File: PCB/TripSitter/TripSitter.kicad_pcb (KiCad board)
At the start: 6 copper layers, 177 parts, among them IC1 MT25QL256ABA1EW9-0SIT, IC2 MT41J128M16JT-125_K, IC4 IP4220CZ6, J1 Conn_ARM_JTAG_SWD_20, J2 DE15_Plug_HighDensity_Mountin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, J3 Conn_ARM_JTAG_SWD_20, J4 USB_B_Micro, J5 Jack-DC, J6 EFM32_PinHeader_PortE, J7 HDMI_A_1.4, J8 USB3_B_Micro, SW1 SW_Push_Open, SW2 SW_DPDT_x2, SW3 SW_DIP_x05, U1 XC7A100T-FGG484, U2 TPS54325_PWP_14, U3 IS62WVS2568FBLL-20NLI, U4 EFM32GG11B420F2048GQ100, U5 TPS54294PWP, U6 IS62WVS2568FBLL-20NLI, U7 TPD12S520DBT, X1 XO53 100Mhz, Y1 48MHz

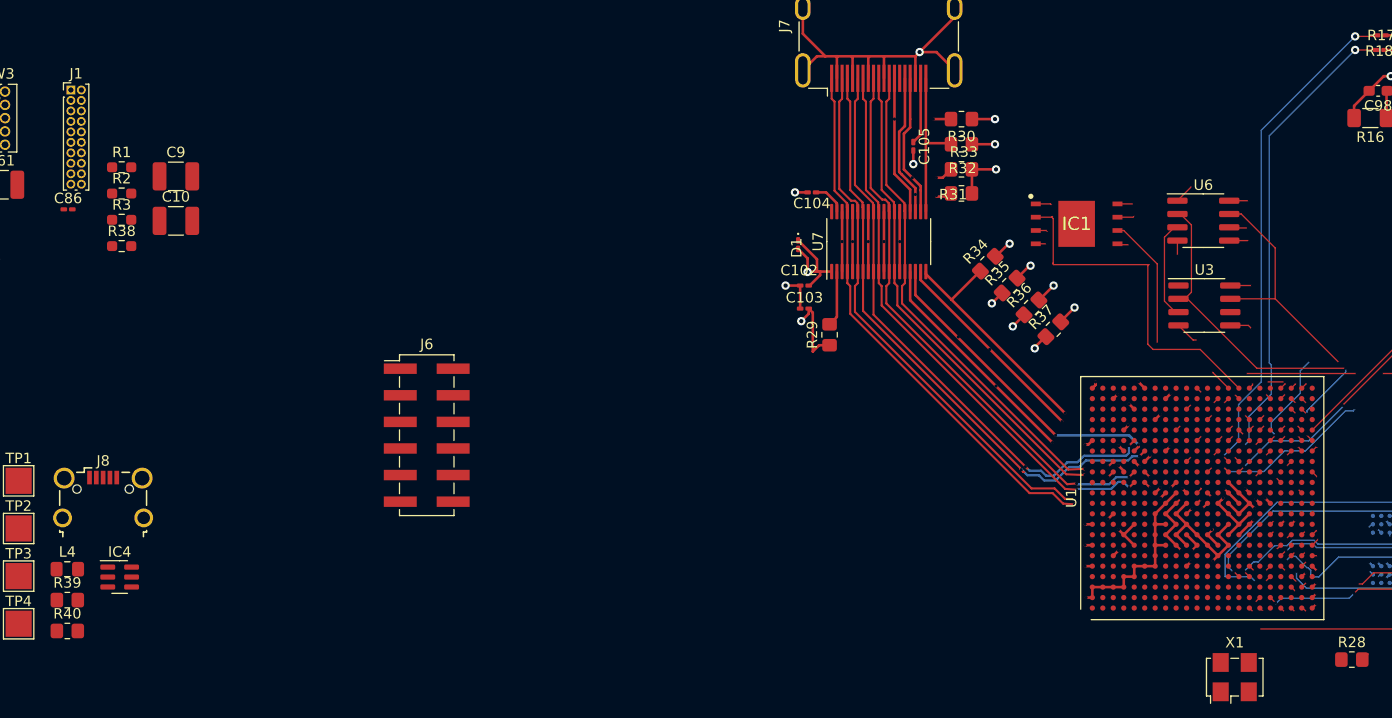
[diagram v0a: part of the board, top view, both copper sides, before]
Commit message: add missing tracks on hdmi
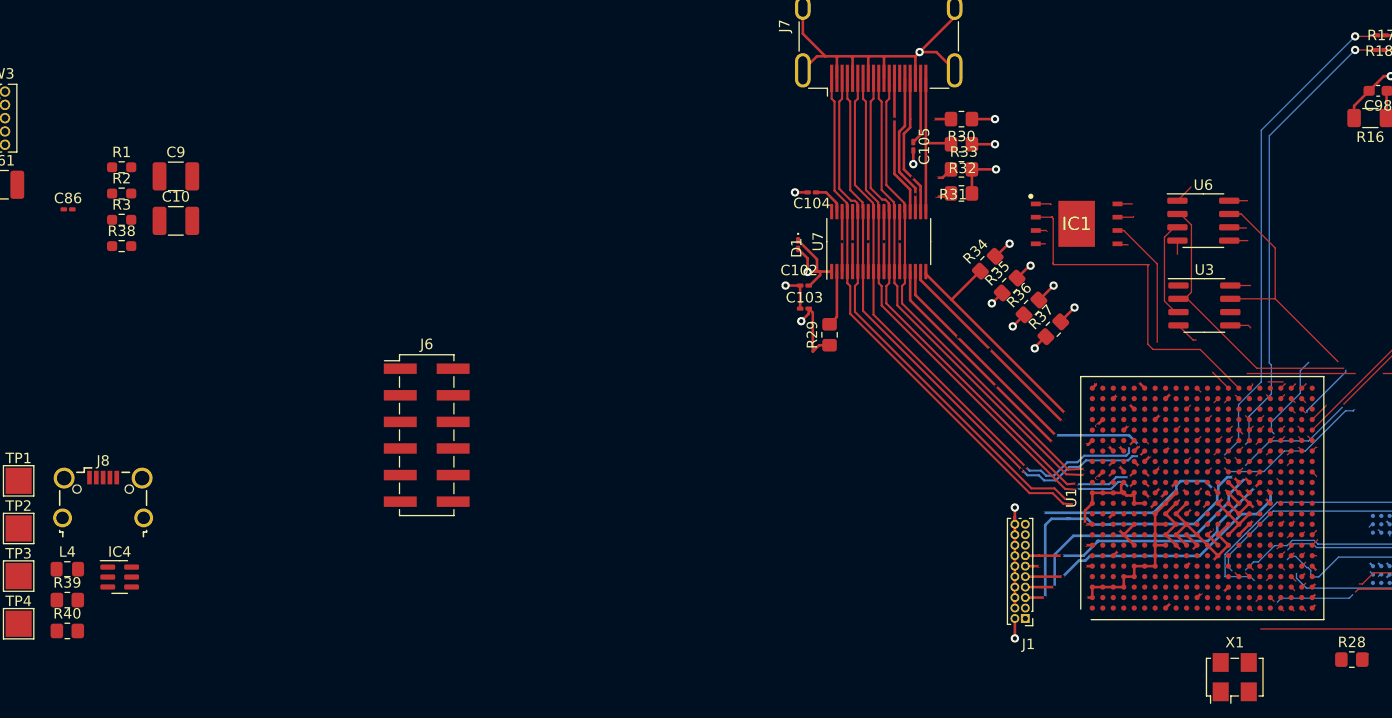
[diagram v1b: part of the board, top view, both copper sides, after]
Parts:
- moved J1 104.2 mm to (213.9, 75.4), turned to 180 degrees
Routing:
- net GND: track 161.7 -> 193.1 mm, vias 44 -> 54
- net Net-(J1-TDI): track 0.00 -> 31.1 mm, vias 0 -> 2
- net Net-(J1-TCK/SWDCLK): track 0.00 -> 28.6 mm, vias 0 -> 2
- net Net-(J1-TMS/SWDIO): track 0.00 -> 28.2 mm, vias 0 -> 2
- net Net-(J1-TDO/SWO): track 0.00 -> 25.8 mm, vias 0 -> 2
- net FPGA_PROGRAM_B: track 0.00 -> 18.7 mm, vias 0 -> 2
- net FPGA_DONE: track 0.00 -> 12.6 mm, vias 0 -> 2
- net +3V3: track 33.9 -> 36.8 mm, vias 28 -> 30
- net +3.3V: track 6.22 -> 7.07 mm, vias 4 -> 5
- net /FPGA Artix-7 100T 1FGG484C/VGA connector/VGA_VSync: track 44.4 -> 45.1 mm

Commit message: Copy/Add power layout
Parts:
- added SW2: SW_DPDT_x2, Button_Switch_SMD:SW_DPDT_CK_JS202011JCQN, F.Cu at (33.9, 48.3)
- moved C101 188.7 mm to (246.1, 145.6)
- moved C28 188.7 mm to (240.5, 138.6)
- moved C30 188.7 mm to (240.5, 140.3)
- moved C31 188.7 mm to (240.5, 142.1)
- moved C32 188.7 mm to (240.5, 143.8)
- moved C42 188.7 mm to (240.5, 145.6)
- moved C43 188.7 mm to (240.5, 147.3)
- moved C44 188.7 mm to (243.3, 138.6)
- moved C45 188.7 mm to (243.3, 140.3)
- moved C80 188.7 mm to (243.3, 142.1)
- moved C81 188.7 mm to (243.3, 143.8)
- moved C82 188.7 mm to (243.3, 145.6)
- moved C83 188.7 mm to (243.3, 147.3)
- moved C90 188.7 mm to (246.1, 138.6)
- moved C91 188.7 mm to (246.1, 140.3)
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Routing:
- net /PCB Power System/5V0: track 0.00 -> 123.7 mm, vias 0 -> 2
- net GND: track 193.1 -> 286.3 mm, vias 54 -> 85
- net /PCB Power System/1V8: track 0.00 -> 75.8 mm, vias 0 -> 1
- net /PCB Power System/1V0: track 0.00 -> 50.8 mm, vias 0 -> 1
- net Net-(U2-PG): track 0.00 -> 31.2 mm
- net /PCB Power System/1V5: track 0.00 -> 26.1 mm, vias 0 -> 1
- net /PCB Power System/3V3: track 0.00 -> 24.8 mm, vias 0 -> 1
- net Net-(U5-VFB2): track 0.00 -> 17.3 mm
- net Net-(U5-EN2): track 0.00 -> 15.5 mm
- net Net-(J4-VBUS): track 0.00 -> 10.7 mm
- net Net-(U2-VREG5): track 0.00 -> 10.3 mm
- net Net-(U2-VFB): track 0.00 -> 8.60 mm
- net Net-(SW2A-C): track 0.00 -> 8.24 mm
- net Net-(U5-VREG5): track 0.00 -> 5.45 mm
- net Net-(U5-SW2): track 0.00 -> 4.12 mm
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
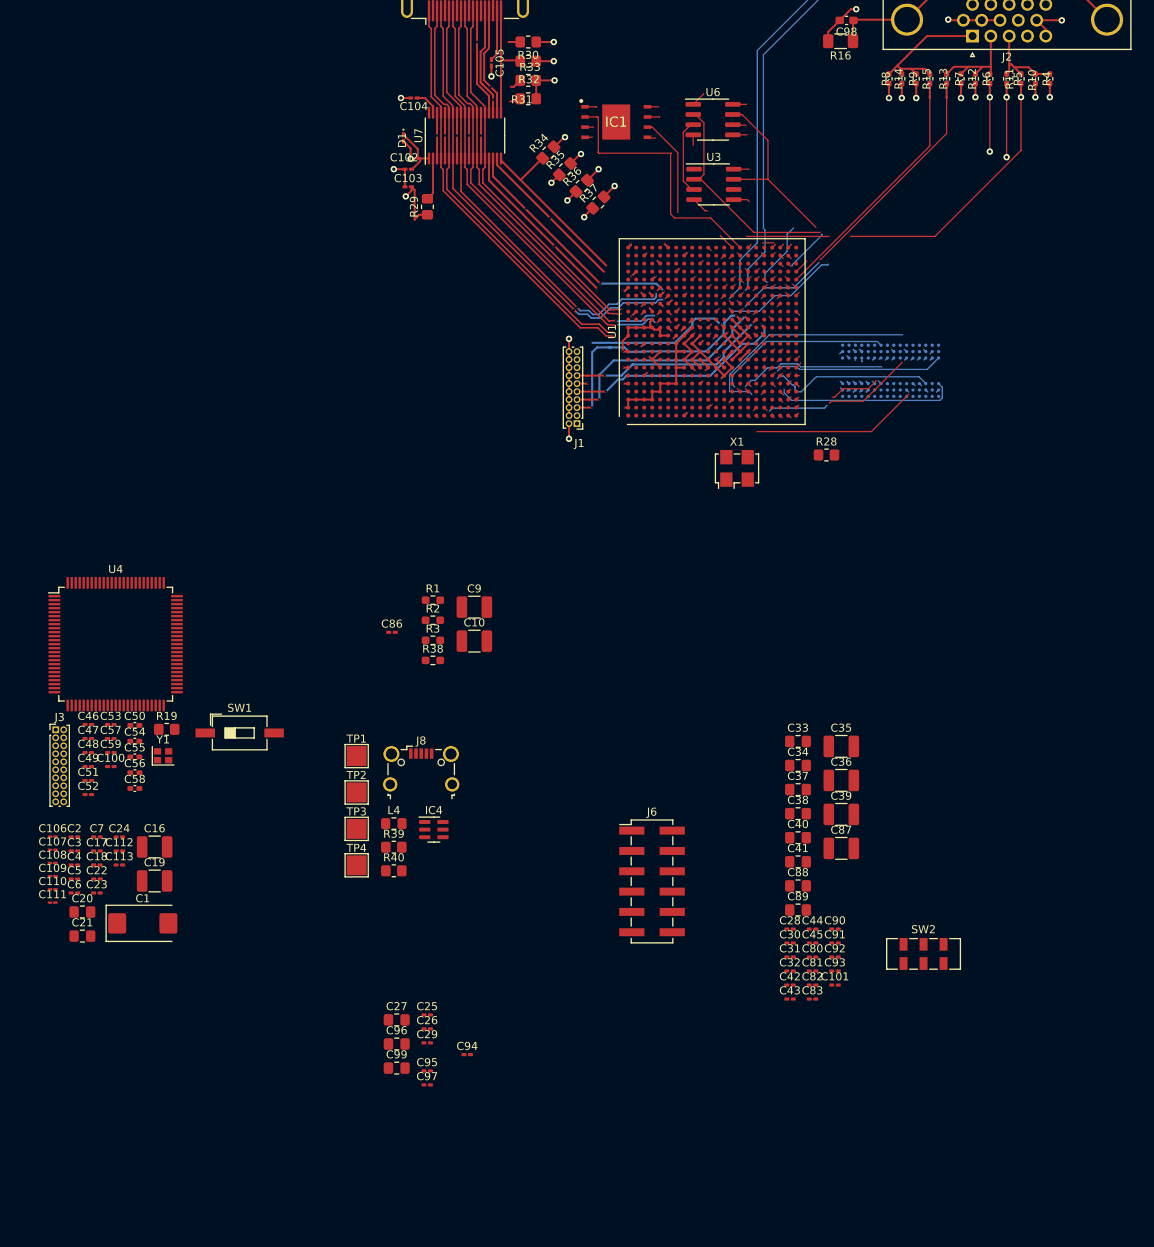
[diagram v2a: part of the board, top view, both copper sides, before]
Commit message: Add USB and JTAG debug for EFM
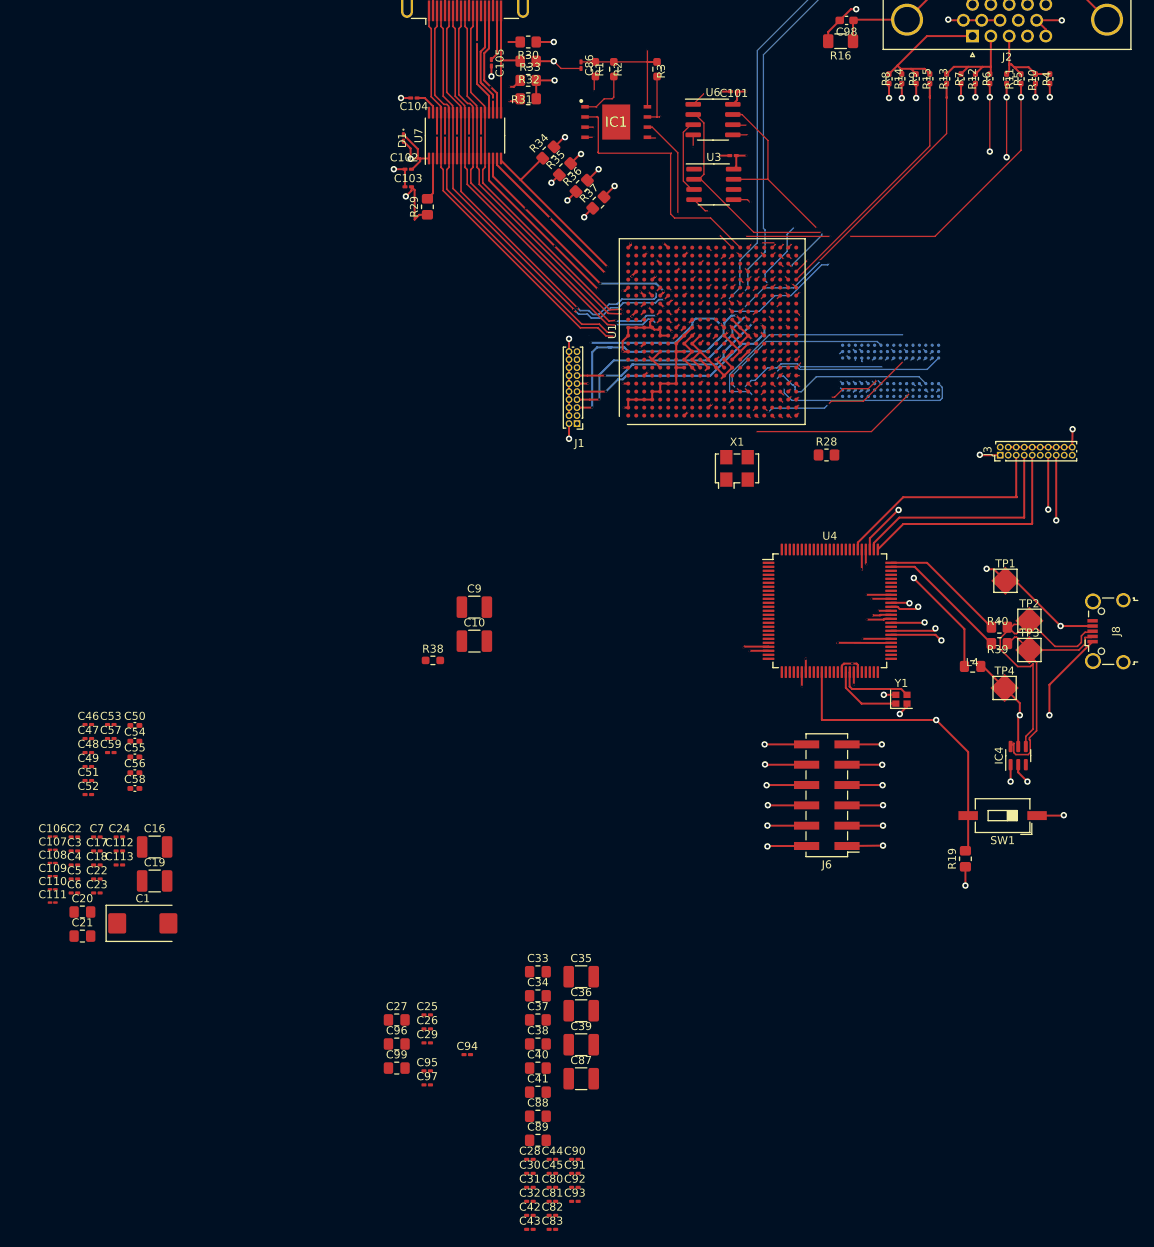
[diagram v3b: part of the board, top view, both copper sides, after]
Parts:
- removed the SW2 at (257.2, 141.7)
- moved J3 123.0 mm to (266.8, 79.3), turned to 90 degrees
- moved C101 112.4 mm to (233.5, 33.9), turned to 180 degrees
- moved C100 109.0 mm to (233.4, 41.9), turned to 180 degrees
- moved R19 101.1 mm to (262.4, 129.8), turned to 90 degrees
- moved SW1 95.9 mm to (267.1, 124.4), turned to 180 degrees
- moved Y1 92.6 mm to (254.4, 109.8)
- moved U4 89.4 mm to (245.5, 98.8)
- moved J8 87.5 mm to (280.2, 101.4), turned to 90 degrees
- moved TP3 87.0 mm to (270.4, 103.7)
- moved TP2 86.8 mm to (270.4, 100.0)
- moved TP1 84.0 mm to (267.4, 95.0)
- moved TP4 84.0 mm to (267.4, 108.5)
- moved R40 81.6 mm to (266.7, 100.8)
- moved R39 79.9 mm to (266.7, 102.9), turned to 180 degrees
- moved R3 76.7 mm to (223.9, 31.1), turned to -90 degrees
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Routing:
- net EFM32_RESETN: track 0.00 -> 77.7 mm, vias 0 -> 2
- net /MCU EFM32GG11B420/PF12: track 0.00 -> 58.8 mm, vias 0 -> 4
- net /MCU EFM32GG11B420/PE0_UART0_TX: track 0.00 -> 39.0 mm, vias 0 -> 2
- net /MCU EFM32GG11B420/USB3_micro_ab/D+: track 0.00 -> 36.9 mm
- net /MCU EFM32GG11B420/PE1_UART0_RX: track 0.00 -> 34.4 mm, vias 0 -> 2
- net /MCU EFM32GG11B420/MCU_EXTIO_PC4: track 0.00 -> 34.4 mm, vias 0 -> 2
- net /MCU EFM32GG11B420/PE_6: track 0.00 -> 34.3 mm, vias 0 -> 2
- net /MCU EFM32GG11B420/MCU_EXTIO_PC6: track 0.00 -> 34.3 mm, vias 0 -> 2
- net /MCU EFM32GG11B420/PE_7: track 0.00 -> 34.0 mm, vias 0 -> 2
- net GND: track 286.3 -> 320.1 mm, vias 85 -> 94
- net +3.3V: track 7.07 -> 40.7 mm, vias 5 -> 10
- net /MCU EFM32GG11B420/MCU_EXTIO_PC7: track 0.00 -> 33.5 mm, vias 0 -> 2
- net /MCU EFM32GG11B420/EBI_ARDY: track 0.00 -> 32.2 mm, vias 0 -> 2
- net /MCU EFM32GG11B420/PE2_UART0_CTS: track 0.00 -> 31.3 mm, vias 0 -> 2
- net /MCU EFM32GG11B420/USB3_micro_ab/D-: track 0.00 -> 31.2 mm
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
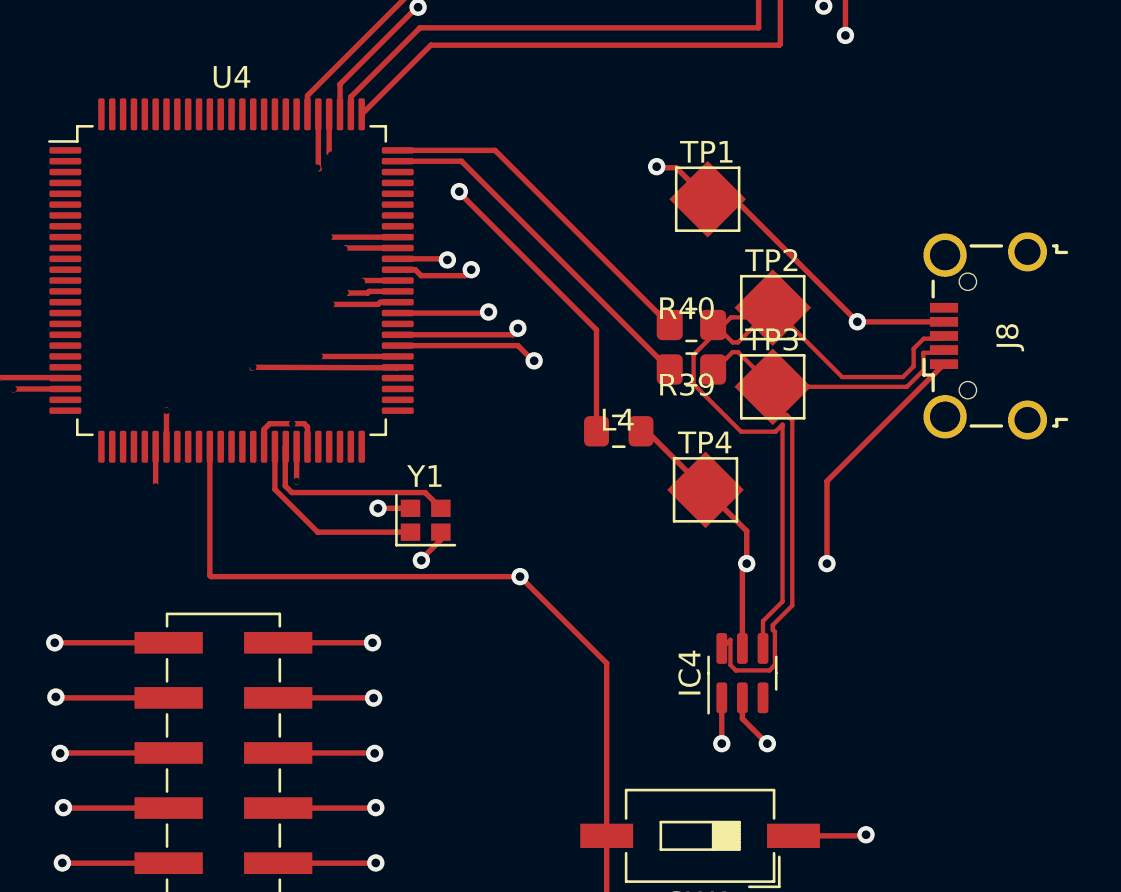
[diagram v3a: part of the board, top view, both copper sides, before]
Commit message: change usb footprint to usb3 footprint
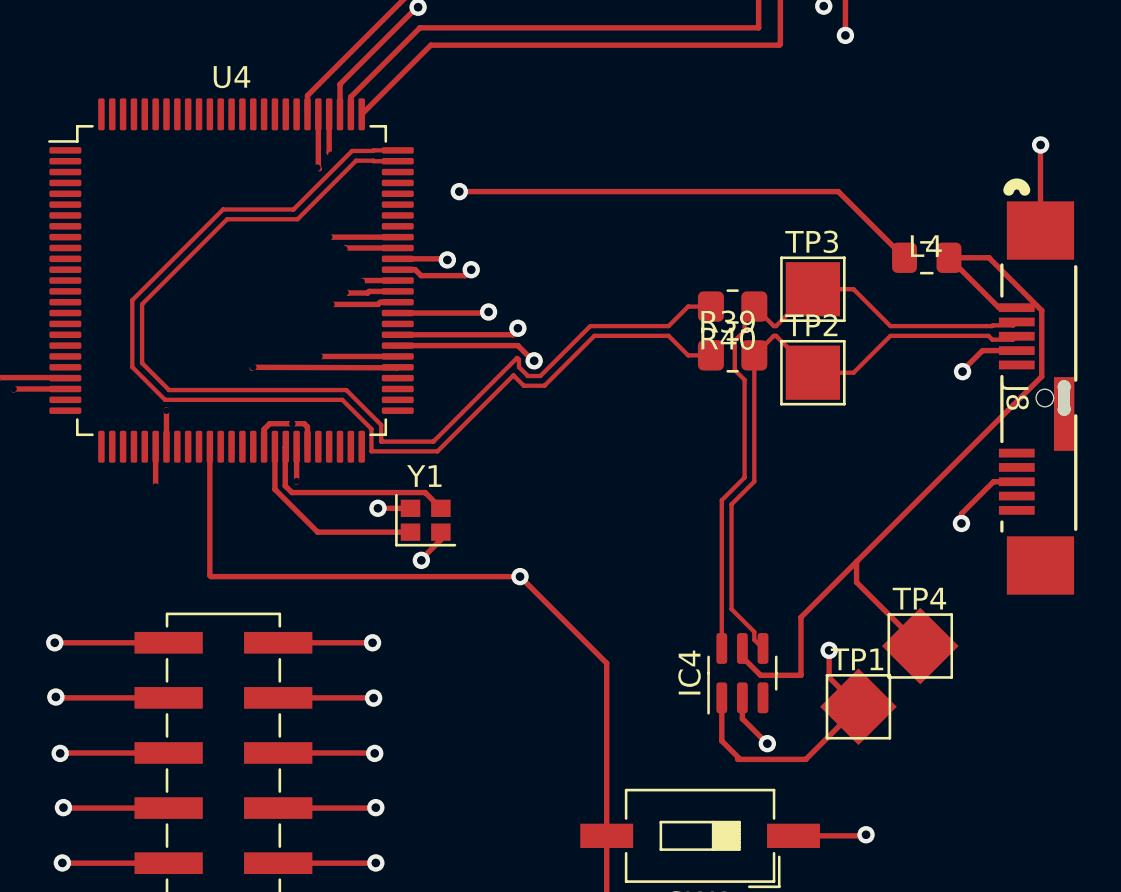
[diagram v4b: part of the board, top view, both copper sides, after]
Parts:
- J8: footprint Connector_USB:USB_Micro-B_Wuerth_629105150521_CircularHoles -> footprints:CONN_897-10-010-00-300002_MIM
- moved TP1 24.4 mm to (274.4, 118.5)
- moved L4 16.3 mm to (277.6, 97.8)
- moved TP4 12.2 mm to (277.2, 115.7)
- moved TP3 4.87 mm to (272.3, 99.2)
- moved J8 3.78 mm to (282.7, 104.2), turned to -90 degrees
- moved TP2 3.52 mm to (272.3, 103.0)
- moved R39 3.47 mm to (268.6, 100.0)
- moved R40 2.36 mm to (268.6, 102.2)
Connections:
- net /MCU EFM32GG11B420/PF10 renamed /MCU EFM32GG11B420/PF11-
- net /MCU EFM32GG11B420/PF11 renamed /MCU EFM32GG11B420/PF11+
- D1 pad 1: +5V -> /FPGA Artix-7 100T 1FGG484C/HDMI Connector/5V_2
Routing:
- net /MCU EFM32GG11B420/PF11+: track 15.9 -> 50.0 mm
- net /MCU EFM32GG11B420/PF11-: track 16.5 -> 48.9 mm
- net /MCU EFM32GG11B420/PF12: track 58.8 -> 34.1 mm, vias 4 -> 3
- net /MCU EFM32GG11B420/USB3_micro_ab/VBUS: track 27.6 -> 39.3 mm, vias 2 -> 0
- net /MCU EFM32GG11B420/USB3_micro_ab/D+: track 36.9 -> 28.6 mm
- net /MCU EFM32GG11B420/VBUS: track 24.9 -> 33.1 mm
- net GND: track 320.1 -> 327.9 mm, vias 94 -> 96
